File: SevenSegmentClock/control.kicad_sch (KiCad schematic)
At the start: 1 part, among them U11 ESP8266

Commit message: Modifying code to use direct port manipulation
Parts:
- U11: footprint ESP8266:ESP12F-Devkit-V3 -> ESP8266:NodeMCU1.0(12-E)
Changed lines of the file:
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@@
       (effects (font (size 1.27 1.27)) (justify left))
     )
-    (property "Footprint" "ESP8266:ESP12F-Devkit-V3" (id 2) (at 150.749 77.47 0)
+    (property "Footprint" "ESP8266:NodeMCU1.0(12-E)" (id 2) (at 150.749 77.47 0)
       (effects (font (size 1.27 1.27)) hide)
     )

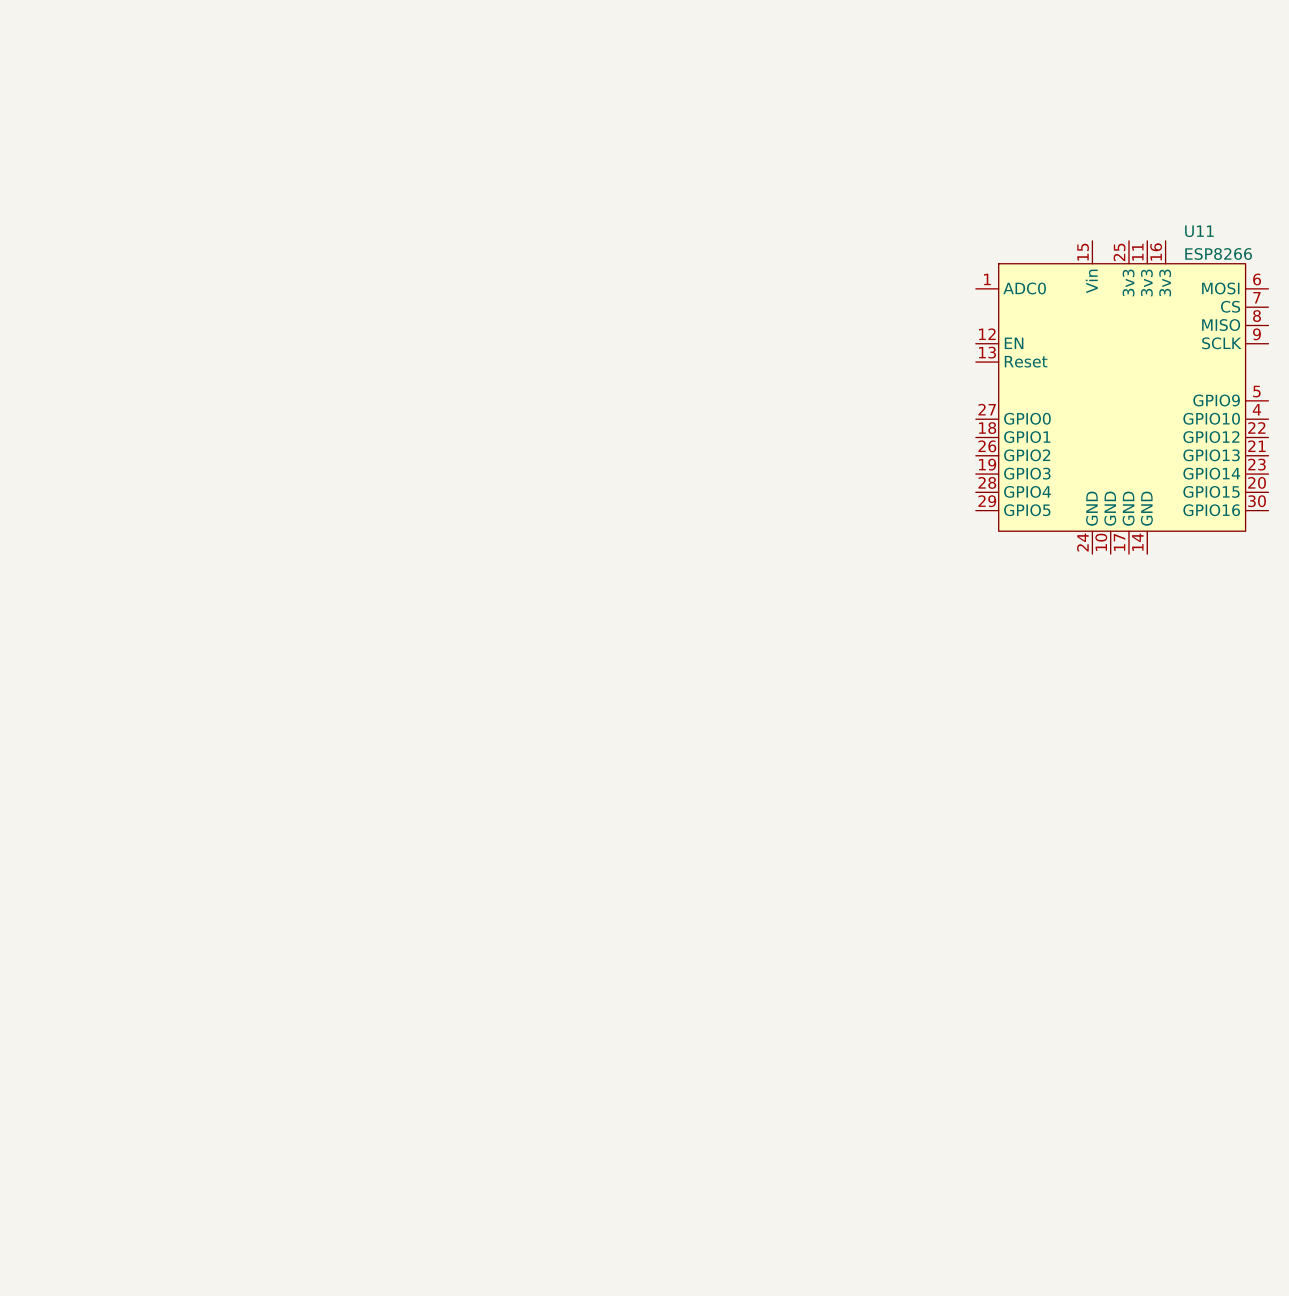
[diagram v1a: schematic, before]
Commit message: Adding two more displays to show a degree and a percent symbols
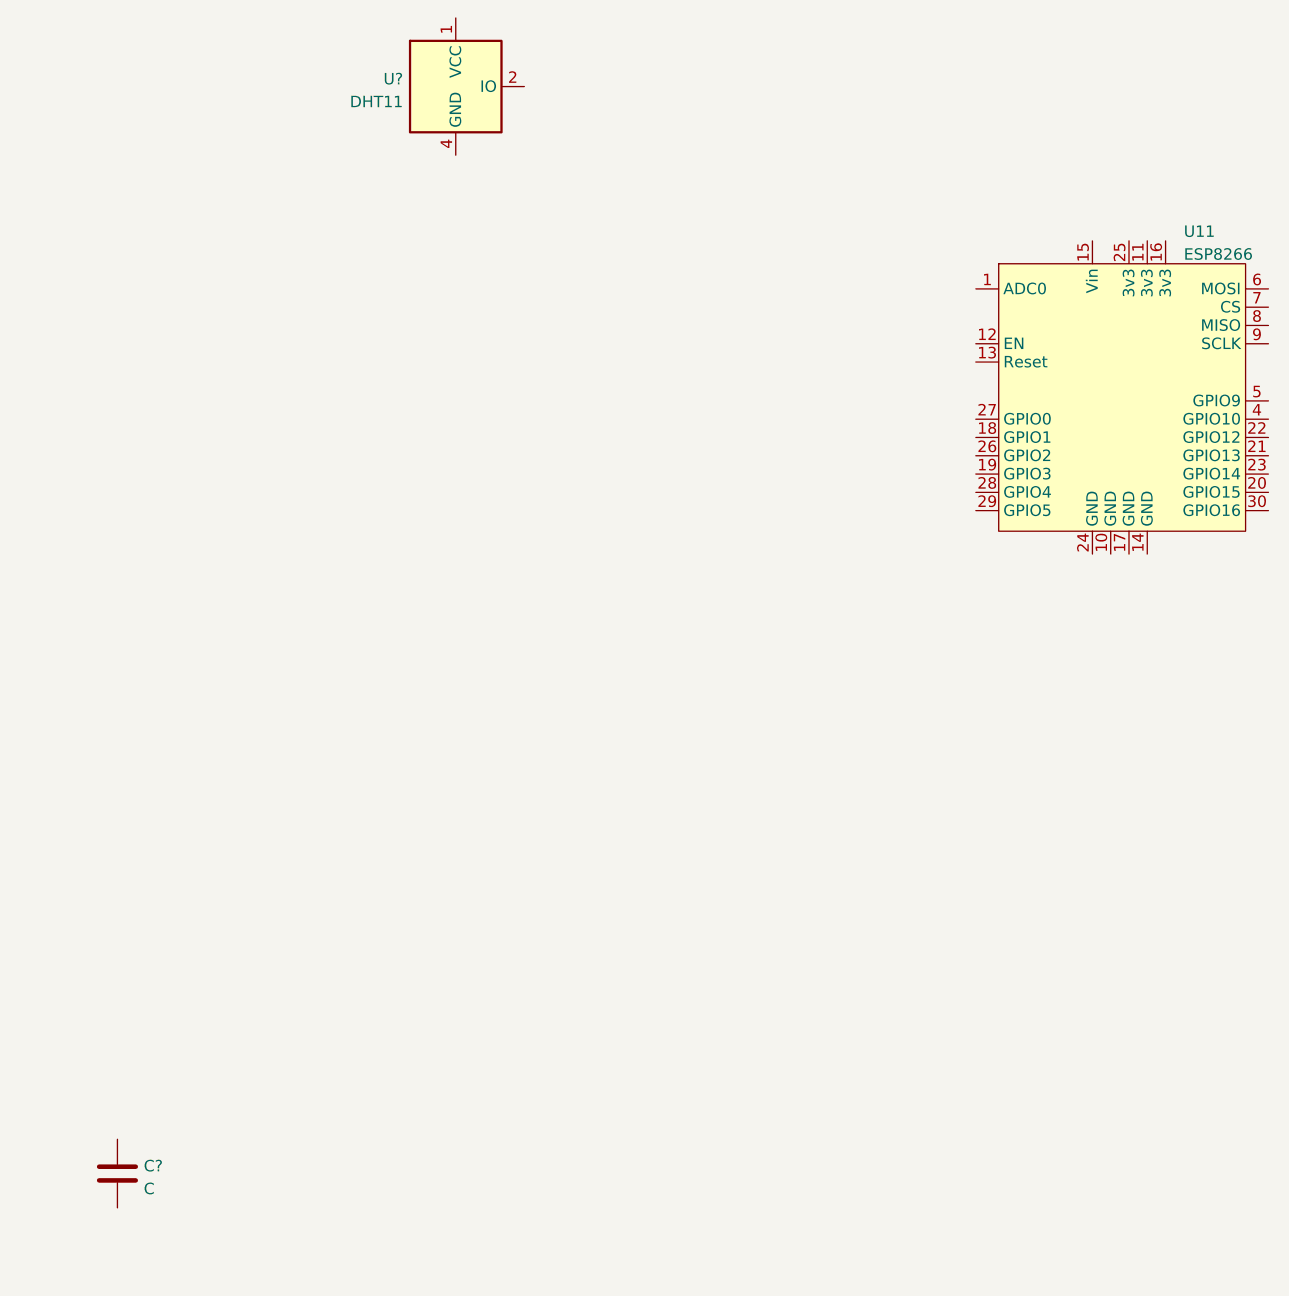
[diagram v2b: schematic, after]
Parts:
- added C?: C, symbol Device:C
- added U?: DHT11, Sensor:Aosong_DHT11_5.5x12.0_P2.54mm, symbol Sensor:DHT11
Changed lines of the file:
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@@
 (kicad_sch (version 20211123) (generator eeschema)
   (paper "A4")
+  (symbol (lib_id "Sensor:DHT11") (at 128.524 58.293 0) (unit 1)
+    (in_bom yes) (on_board yes) (fields_autoplaced)
+    (property "Reference" "U?" (id 0) (at 122.6821 57.4583 0)
+      (effects (font (size 1.27 1.27)) (justify right))
+    )
+    (property "Value" "DHT11" (id 1) (at 122.6821 59.9952 0)
+      (effects (font (size 1.27 1.27)) (justify right))
+    )
+    (property "Footprint" "Sensor:Aosong_DHT11_5.5x12.0_P2.54mm" (id 2) (at 128.524 68.453 0)
+      (effects (font (size 1.27 1.27)) hide)
+    )
+    (property "Datasheet" "http://akizukidenshi.com/download/ds/aosong/DHT11.pdf" (id 3) (at 132.334 51.943 0)
+      (effects (font (size 1.27 1.27)) hide)
+    )
+    (pin "1")
+    (pin "2")
+    (pin "3")
+    (pin "4")
+  )
+  (symbol (lib_id "Device:C") (at 90.932 179.07 0) (unit 1)
+    (in_bom yes) (on_board yes) (fields_autoplaced)
+    (property "Reference" "C?" (id 0) (at 93.853 178.2353 0)
+      (effects (font (size 1.27 1.27)) (justify left))
+    )
+    (property "Value" "C" (id 1) (at 93.853 180.7722 0)
+      (effects (font (size 1.27 1.27)) (justify left))
+    )
+    (property "Footprint" "" (id 2) (at 91.8972 182.88 0)
+      (effects (font (size 1.27 1.27)) hide)
+    )
+    (property "Datasheet" "~" (id 3) (at 90.932 179.07 0)
+      (effects (font (size 1.27 1.27)) hide)
+    )
+    (pin "1")
+    (pin "2")
+  )
   (symbol (lib_id "Library:ESP8266") (at 202.311 92.71 0) (unit 1)
     (in_bom yes) (on_board yes) (fields_autoplaced)

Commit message: Adding the control schematic and fixing Eletrical Rules Checks
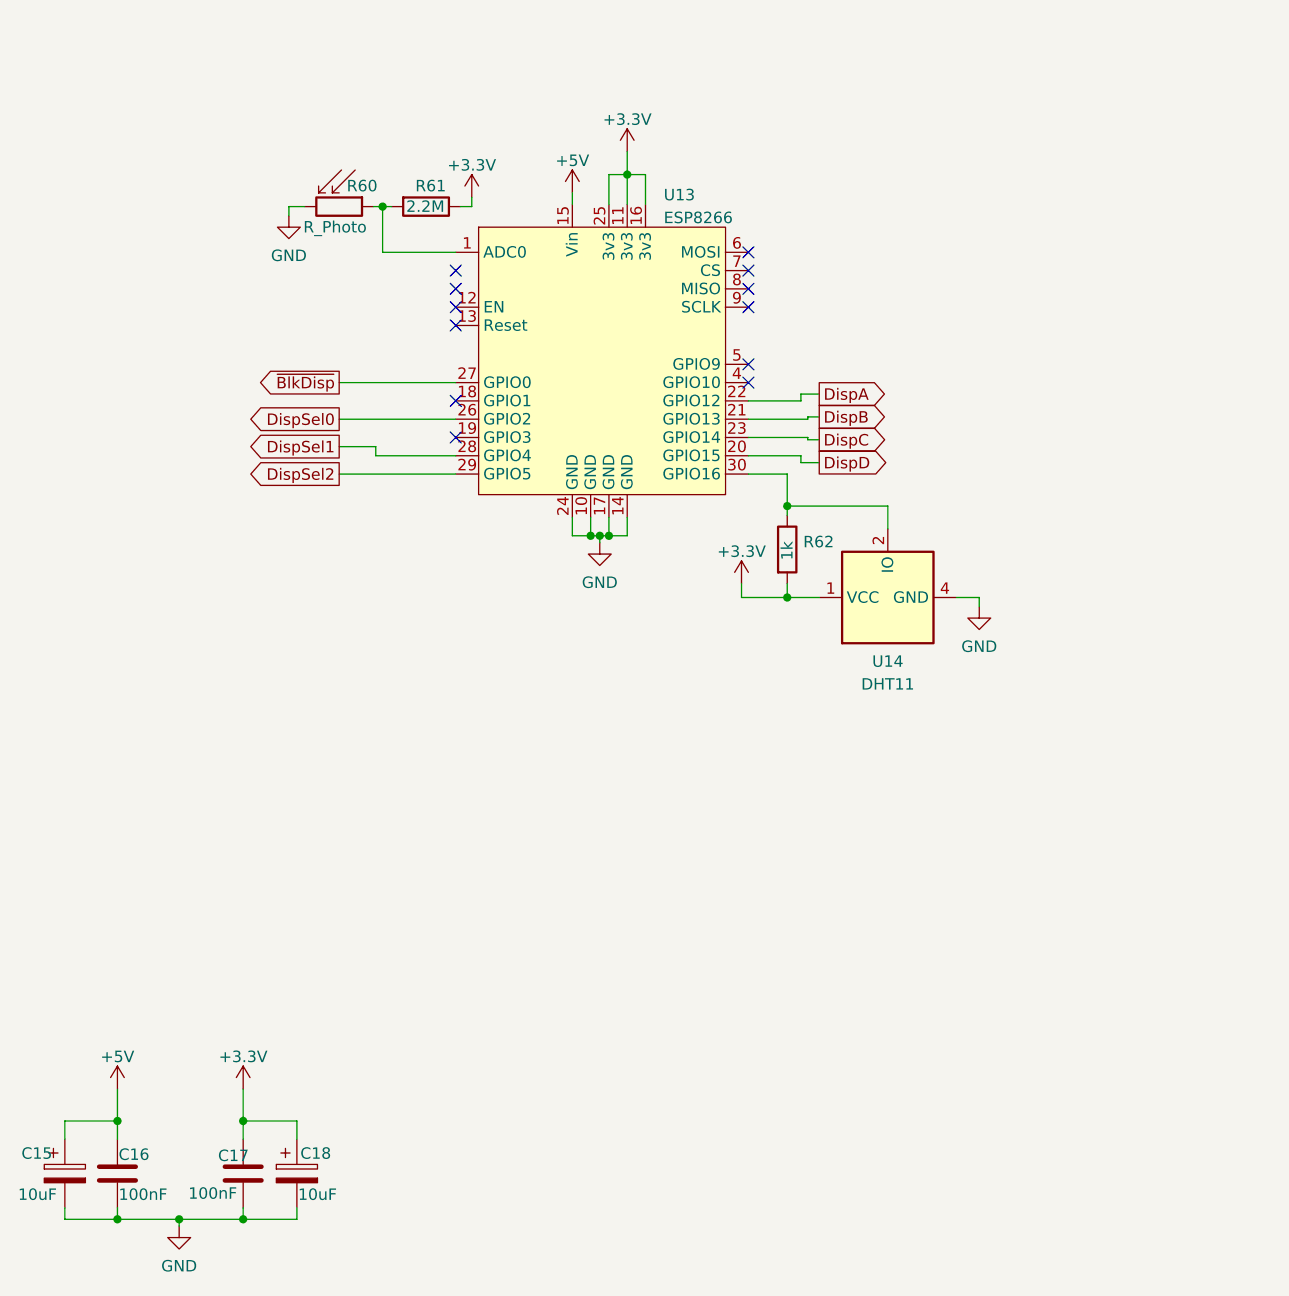
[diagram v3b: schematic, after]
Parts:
- added C15, C18: 10uF, symbol Device:C_Polarized
- added C17: 100nF, symbol Device:C
- added R60: R_Photo, symbol Device:R_Photo
- added R61: 2.2M, symbol Device:R
- added R62: 1k, symbol Device:R
- C16: renamed from C?; value C -> 100nF
- gave numbers to parts that had none: 1
- renumbered U11 to U13
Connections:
- net +3.3V: now reaches U14.1 (VCC)
- net +3.3V: now also U13.11 (3v3), U13.16 (3v3), U13.25 (3v3), C17.1, C18.1, R61.1, R62.2
- net at U14.2 (IO): now also U13.30 (GPIO16), R62.1
- net GND: now reaches U14.4 (GND)
- net GND: now also C16.2, U13.10 (GND), U13.14 (GND), U13.17 (GND), U13.24 (GND), C15.2, C17.2, C18.2, R60.2
- net +5V: now reaches C16.1
- net +5V: now also U13.15 (Vin), C15.1
- net at U13.1 (ADC0): now also R60.1, R61.2
- net DispD: now reaches U13.20 (GPIO15)
- net DispB: now reaches U13.21 (GPIO13)
- net DispA: now reaches U13.22 (GPIO12)
- net DispC: now reaches U13.23 (GPIO14)
- net DispSel0: now reaches U13.26 (GPIO2)
- net ~{BlkDisp}: now reaches U13.27 (GPIO0)
- net DispSel1: now reaches U13.28 (GPIO4)
- net DispSel2: now reaches U13.29 (GPIO5)
- no-connect marks 0 -> 12
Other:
- moved on the sheet: U13, U14

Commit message: Assigning footprints
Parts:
- added C25: 4.7uF, Capacitor_THT:CP_Radial_D6.3mm_P2.50mm, symbol Device:C_Polarized
- C15: value 10uF -> 4.7uF; footprint (none) -> Capacitor_THT:CP_Radial_D6.3mm_P2.50mm
- C16, C17: footprint (none) -> Capacitor_THT:C_Disc_D5.0mm_W2.5mm_P5.00mm
- C18: value 10uF -> 47uF; footprint (none) -> Capacitor_THT:CP_Radial_D6.3mm_P2.50mm
- R60: footprint (none) -> OptoDevice:R_LDR_4.9x4.2mm_P2.54mm_Vertical
- R61: footprint (none) -> Resistor_THT:R_Axial_DIN0207_L6.3mm_D2.5mm_P10.16mm_Horizontal
- R62: footprint (none) -> Resistor_SMD:R_1206_3216Metric_Pad1.30x1.75mm_HandSolder
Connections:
- net +3.3V: now also C25.1
- net GND: now also C25.2
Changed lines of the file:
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@@
   (junction (at 144.526 108.204) (diameter 0) (color 0 0 0 0)
+  )
+  (junction (at 110.871 173.228) (diameter 0) (color 0 0 0 0)
+  )
+  (junction (at 110.871 184.15) (diameter 0) (color 0 0 0 0)
   )
   (junction (at 120.396 71.628) (diameter 0) (color 0 0 0 0)
@@
     (stroke (width 0) (type default) (color 0 0 0 0))
   )
+  (wire (pts (xy 116.713 173.228) (xy 110.871 173.228))
+    (stroke (width 0) (type default) (color 0 0 0 0))
+  )
   (wire (pts (xy 120.396 71.628) (xy 120.396 76.708))
     (stroke (width 0) (type default) (color 0 0 0 0))
@@
     (stroke (width 0) (type default) (color 0 0 0 0))
   )
+  (wire (pts (xy 116.713 182.88) (xy 116.713 184.15))
+    (stroke (width 0) (type default) (color 0 0 0 0))
+  )
   (wire (pts (xy 166.878 93.218) (xy 166.878 92.456))
     (stroke (width 0) (type default) (color 0 0 0 0))
@@
     (stroke (width 0) (type default) (color 0 0 0 0))
   )
+  (wire (pts (xy 116.713 184.15) (xy 110.871 184.15))
+    (stroke (width 0) (type default) (color 0 0 0 0))
+  )
   (wire (pts (xy 145.542 106.172) (xy 145.542 108.204))
     (stroke (width 0) (type default) (color 0 0 0 0))
@@
   )
   (wire (pts (xy 110.871 173.228) (xy 104.902 173.228))
+    (stroke (width 0) (type default) (color 0 0 0 0))
+  )
+  (wire (pts (xy 116.713 175.26) (xy 116.713 173.228))
     (stroke (width 0) (type default) (color 0 0 0 0))
   )
@@
       (effects (font (size 1.27 1.27)) (justify left))
     )
-    (property "Footprint" "" (id 2) (at 109.22 72.898 90)
+    (property "Footprint" "OptoDevice:R_LDR_4.9x4.2mm_P2.54mm_Vertical" (id 2) (at 109.22 72.898 90)
       (effects (font (size 1.27 1.27)) (justify left) hide)
     )
@@
   (symbol (lib_id "Device:C_Polarized") (at 85.09 179.07 0) (unit 1)
     (in_bom yes) (on_board yes)
-    (property "Reference" "C15" (id 0) (at 80.264 176.8383 0)
-      (effects (font (size 1.27 1.27)) (justify left))
-    )
-    (property "Value" "10uF" (id 1) (at 79.883 181.4072 0)
-      (effects (font (size 1.27 1.27)) (justify left))
-    )
-    (property "Footprint" "" (id 2) (at 86.0552 182.88 0)
+    (property "Reference" "C15" (id 0) (at 84.963 176.9653 0)
+      (effects (font (size 1.27 1.27)) (justify left))
+    )
+    (property "Value" "4.7uF" (id 1) (at 79.883 181.4072 0)
+      (effects (font (size 1.27 1.27)) (justify left))
+    )
+    (property "Footprint" "Capacitor_THT:CP_Radial_D6.3mm_P2.50mm" (id 2) (at 86.0552 182.88 0)
       (effects (font (size 1.27 1.27)) hide)
     )
@@
       (effects (font (size 1.27 1.27)) (justify left))
     )
-    (property "Footprint" "" (id 2) (at 125.222 69.85 90)
+    (property "Footprint" "Resistor_THT:R_Axial_DIN0207_L6.3mm_D2.5mm_P10.16mm_Horizontal" (id 2) (at 125.222 69.85 90)
       (effects (font (size 1.27 1.27)) hide)
     )
@@
   (symbol (lib_id "Device:C") (at 104.902 179.07 0) (unit 1)
     (in_bom yes) (on_board yes)
-    (property "Reference" "C17" (id 0) (at 102.108 177.0923 0)
+    (property "Reference" "C17" (id 0) (at 105.029 177.0923 0)
       (effects (font (size 1.27 1.27)) (justify left))
     )
@@
       (effects (font (size 1.27 1.27)) (justify left))
     )
-    (property "Footprint" "" (id 2) (at 105.8672 182.88 0)
+    (property "Footprint" "Capacitor_THT:C_Disc_D5.0mm_W2.5mm_P5.00mm" (id 2) (at 105.8672 182.88 0)
       (effects (font (size 1.27 1.27)) hide)
     )
@@
       (effects (font (size 1.27 1.27)) (justify left))
     )
-    (property "Footprint" "" (id 2) (at 163.576 109.728 90)
+    (property "Footprint" "Resistor_SMD:R_1206_3216Metric_Pad1.30x1.75mm_HandSolder" (id 2) (at 163.576 109.728 90)
       (effects (font (size 1.27 1.27)) hide)
     )
@@
       (effects (font (size 1.27 1.27)) (justify left))
     )
-    (property "Footprint" "" (id 2) (at 91.8972 182.88 0)
+    (property "Footprint" "Capacitor_THT:C_Disc_D5.0mm_W2.5mm_P5.00mm" (id 2) (at 91.8972 182.88 0)
       (effects (font (size 1.27 1.27)) hide)
     )
@@
   (symbol (lib_id "Device:C_Polarized") (at 110.871 179.07 0) (unit 1)
     (in_bom yes) (on_board yes)
-    (property "Reference" "C18" (id 0) (at 111.252 176.8383 0)
-      (effects (font (size 1.27 1.27)) (justify left))
-    )
-    (property "Value" "10uF" (id 1) (at 110.998 181.4072 0)
-      (effects (font (size 1.27 1.27)) (justify left))
-    )
-    (property "Footprint" "" (id 2) (at 111.8362 182.88 0)
+    (property "Reference" "C18" (id 0) (at 110.871 176.7113 0)
+      (effects (font (size 1.27 1.27)) (justify left))
+    )
+    (property "Value" "47uF" (id 1) (at 110.998 181.4072 0)
+      (effects (font (size 1.27 1.27)) (justify left))
+    )
+    (property "Footprint" "Capacitor_THT:CP_Radial_D6.3mm_P2.50mm" (id 2) (at 111.8362 182.88 0)
       (effects (font (size 1.27 1.27)) hide)
     )
@@
     (pin "1")
   )
+  (symbol (lib_id "Device:C_Polarized") (at 116.713 179.07 0) (unit 1)
+    (in_bom yes) (on_board yes)
+    (property "Reference" "C25" (id 0) (at 117.348 176.8383 0)
+      (effects (font (size 1.27 1.27)) (justify left))
+    )
+    (property "Value" "4.7uF" (id 1) (at 117.348 181.4072 0)
+      (effects (font (size 1.27 1.27)) (justify left))
+    )
+    (property "Footprint" "Capacitor_THT:CP_Radial_D6.3mm_P2.50mm" (id 2) (at 117.6782 182.88 0)
+      (effects (font (size 1.27 1.27)) hide)
+    )
+    (property "Datasheet" "~" (id 3) (at 116.713 179.07 0)
+      (effects (font (size 1.27 1.27)) hide)
+    )
+    (pin "1")
+    (pin "2")
+  )
 )

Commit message: Fixing incorrect footprints
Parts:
- U13: footprint ESP8266:NodeMCU1.0(12-E) -> Library:ESP8266 (NodeMCU_12-E)
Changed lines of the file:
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@@
       (effects (font (size 1.27 1.27)) (justify left))
     )
-    (property "Footprint" "ESP8266:NodeMCU1.0(12-E)" (id 2) (at 92.964 73.406 0)
+    (property "Footprint" "Library:ESP8266 (NodeMCU_12-E)" (id 2) (at 92.964 73.406 0)
       (effects (font (size 1.27 1.27)) hide)
     )

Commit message: WIP: PCB design
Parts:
- C16, C17: footprint Capacitor_THT:C_Disc_D5.0mm_W2.5mm_P5.00mm -> Capacitor_SMD:C_1206_3216Metric_Pad1.33x1.80mm_HandSolder
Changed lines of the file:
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@@
       (effects (font (size 1.27 1.27)) (justify left))
     )
-    (property "Footprint" "Capacitor_THT:C_Disc_D5.0mm_W2.5mm_P5.00mm" (id 2) (at 105.8672 182.88 0)
+    (property "Footprint" "Capacitor_SMD:C_1206_3216Metric_Pad1.33x1.80mm_HandSolder" (id 2) (at 105.8672 182.88 0)
       (effects (font (size 1.27 1.27)) hide)
     )
@@
       (effects (font (size 1.27 1.27)) (justify left))
     )
-    (property "Footprint" "Capacitor_THT:C_Disc_D5.0mm_W2.5mm_P5.00mm" (id 2) (at 91.8972 182.88 0)
+    (property "Footprint" "Capacitor_SMD:C_1206_3216Metric_Pad1.33x1.80mm_HandSolder" (id 2) (at 91.8972 182.88 0)
       (effects (font (size 1.27 1.27)) hide)
     )
